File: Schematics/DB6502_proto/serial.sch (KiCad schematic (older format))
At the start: 21 parts, among them J11 LCD Port, J12 VIA Ports, U17 74AC08, U18 SC26C92, U19 65C22S, U20 74AC04, U21 74AC574, U8 74AC04, U9 74HC21, Y2 3,6864MHz

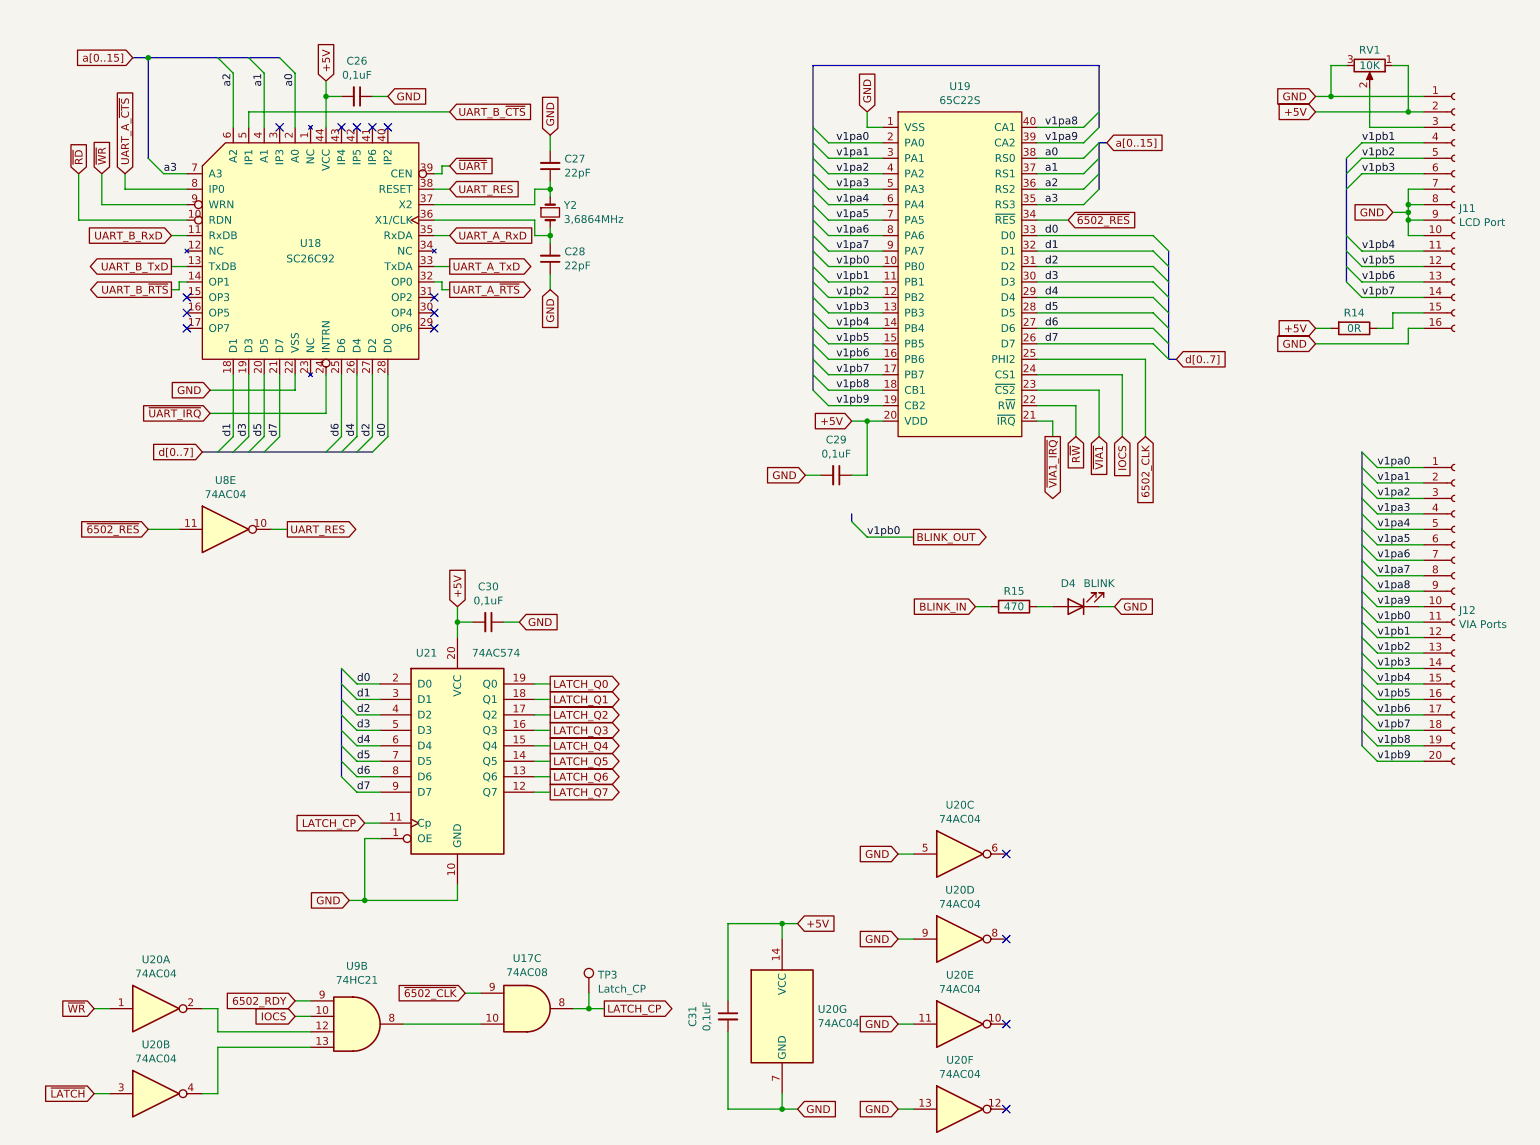
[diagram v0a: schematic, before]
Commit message: Added GPIO section
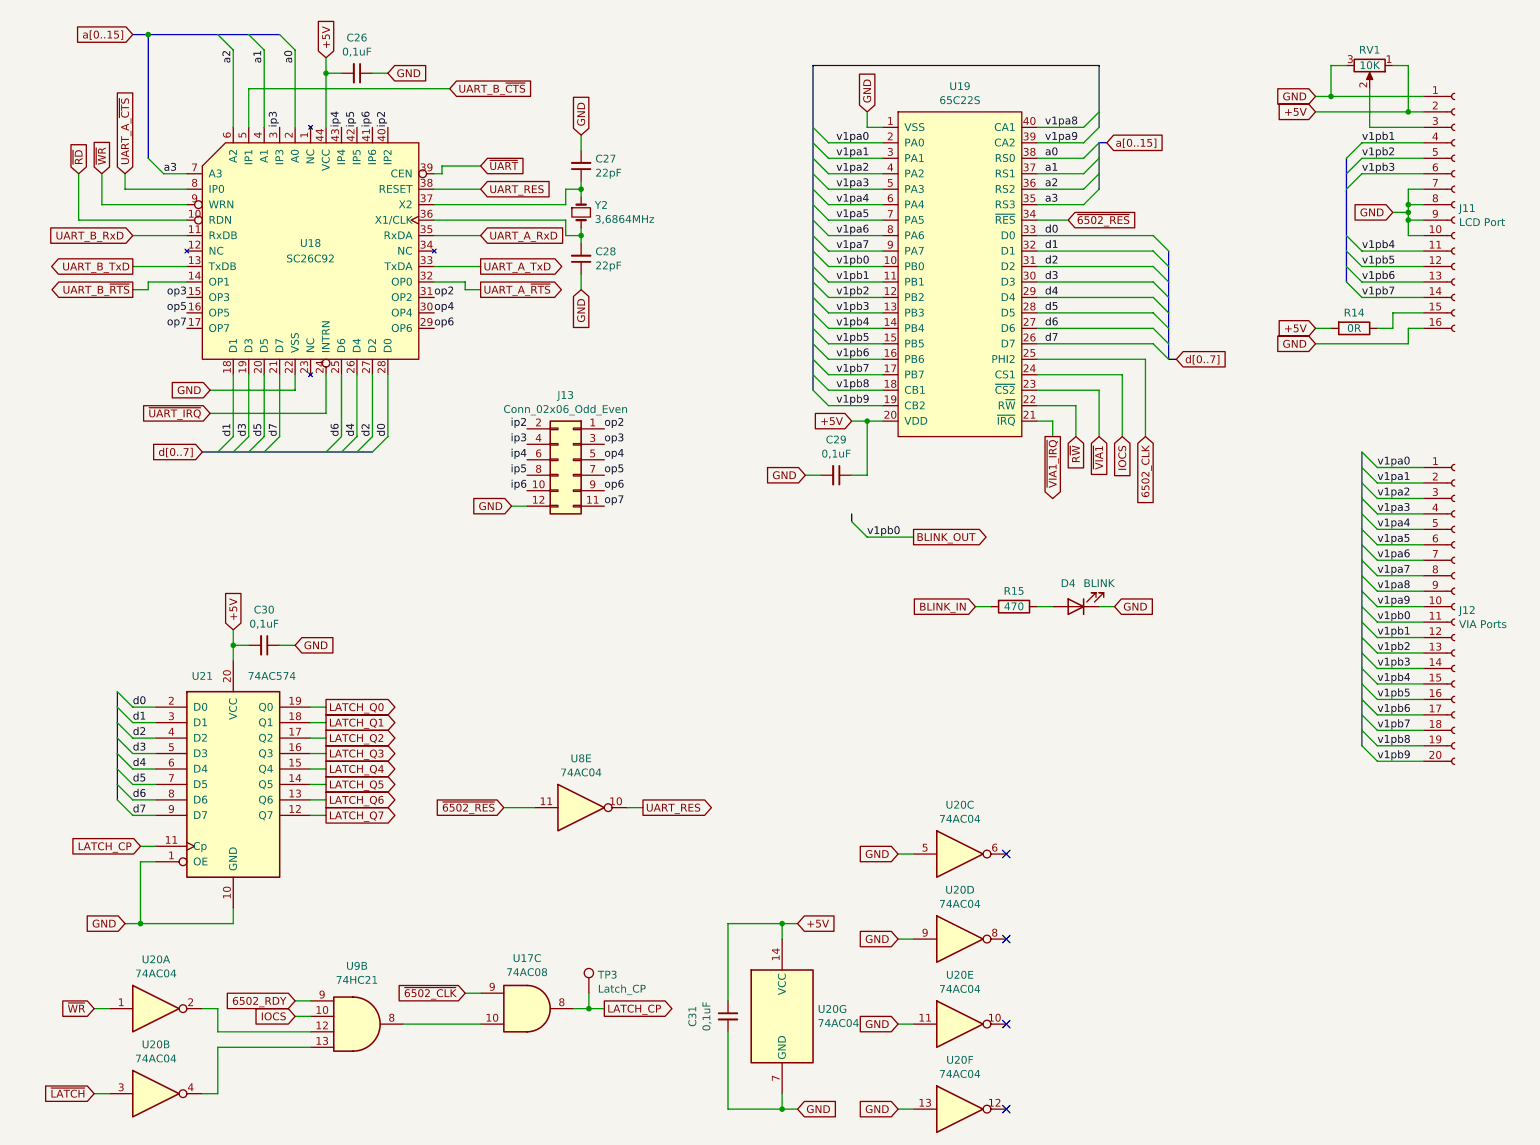
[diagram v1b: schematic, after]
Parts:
- added J13: Conn_02x06_Odd_Even, Connector_PinSocket_2.54mm:PinSocket_2x06_P2.54mm_Vertical, symbol Connector_Generic:Conn_02x06_Odd_Even
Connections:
- net GND: now also J13.12 (Pin_12)
- net op3: now reaches U18.15 (OP3)
- net op3: now also J13.3 (Pin_3)
- net op5: now reaches U18.16 (OP5)
- net op5: now also J13.7 (Pin_7)
- net op7: now reaches U18.17 (OP7)
- net op7: now also J13.11 (Pin_11)
- net op6: now reaches U18.29 (OP6)
- net op6: now also J13.9 (Pin_9)
- net ip3: now reaches U18.3 (IP3)
- net ip3: now also J13.4 (Pin_4)
- net op4: now reaches U18.30 (OP4)
- net op4: now also J13.5 (Pin_5)
- net op2: now reaches U18.31 (OP2)
- net op2: now also J13.1 (Pin_1)
- net ip2: now reaches U18.40 (IP2)
- net ip2: now also J13.2 (Pin_2)
- net ip6: now reaches U18.41 (IP6)
- net ip6: now also J13.10 (Pin_10)
- net ip5: now reaches U18.42 (IP5)
- net ip5: now also J13.8 (Pin_8)
- net ip4: now reaches U18.43 (IP4)
- net ip4: now also J13.6 (Pin_6)
- no-connect marks 15 -> 4
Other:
- moved on the sheet: C26, C27, C28, C30, U21, U8E, Y2

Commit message: Further improvements
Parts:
- J13: value Conn_02x06_Odd_Even -> UART GPIO
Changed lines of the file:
@@
 P 4100 3400
 F 0 "J13" H 4150 3817 50  0000 C CNN
-F 1 "Conn_02x06_Odd_Even" H 4150 3726 50  0000 C CNN
+F 1 "UART GPIO" H 4150 3726 50  0000 C CNN
 F 2 "Connector_PinSocket_2.54mm:PinSocket_2x06_P2.54mm_Vertical" H 4100 3400 50  0001 C CNN
 F 3 "~" H 4100 3400 50  0001 C CNN

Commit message: PCB RC2
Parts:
- C27, C28: footprint Capacitor_THT:C_Disc_D5.0mm_W2.5mm_P2.50mm -> Capacitor_SMD:C_1206_3216Metric_Pad1.33x1.80mm_HandSolder
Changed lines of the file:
@@
 F 0 "C27" H 4058 1454 50  0000 R CNN
 F 1 "22pF" H 4058 1545 50  0000 R CNN
-F 2 "Capacitor_THT:C_Disc_D5.0mm_W2.5mm_P2.50mm" H 4150 1500 50  0001 C CNN
+F 2 "Capacitor_SMD:C_1206_3216Metric_Pad1.33x1.80mm_HandSolder" H 4150 1500 50  0001 C CNN
 F 3 "~" H 4150 1500 50  0001 C CNN
 	1    4150 1500
@@
 F 0 "C28" H 4058 2054 50  0000 R CNN
 F 1 "22pF" H 4058 2145 50  0000 R CNN
-F 2 "Capacitor_THT:C_Disc_D5.0mm_W2.5mm_P2.50mm" H 4150 2100 50  0001 C CNN
+F 2 "Capacitor_SMD:C_1206_3216Metric_Pad1.33x1.80mm_HandSolder" H 4150 2100 50  0001 C CNN
 F 3 "~" H 4150 2100 50  0001 C CNN
 	1    4150 2100

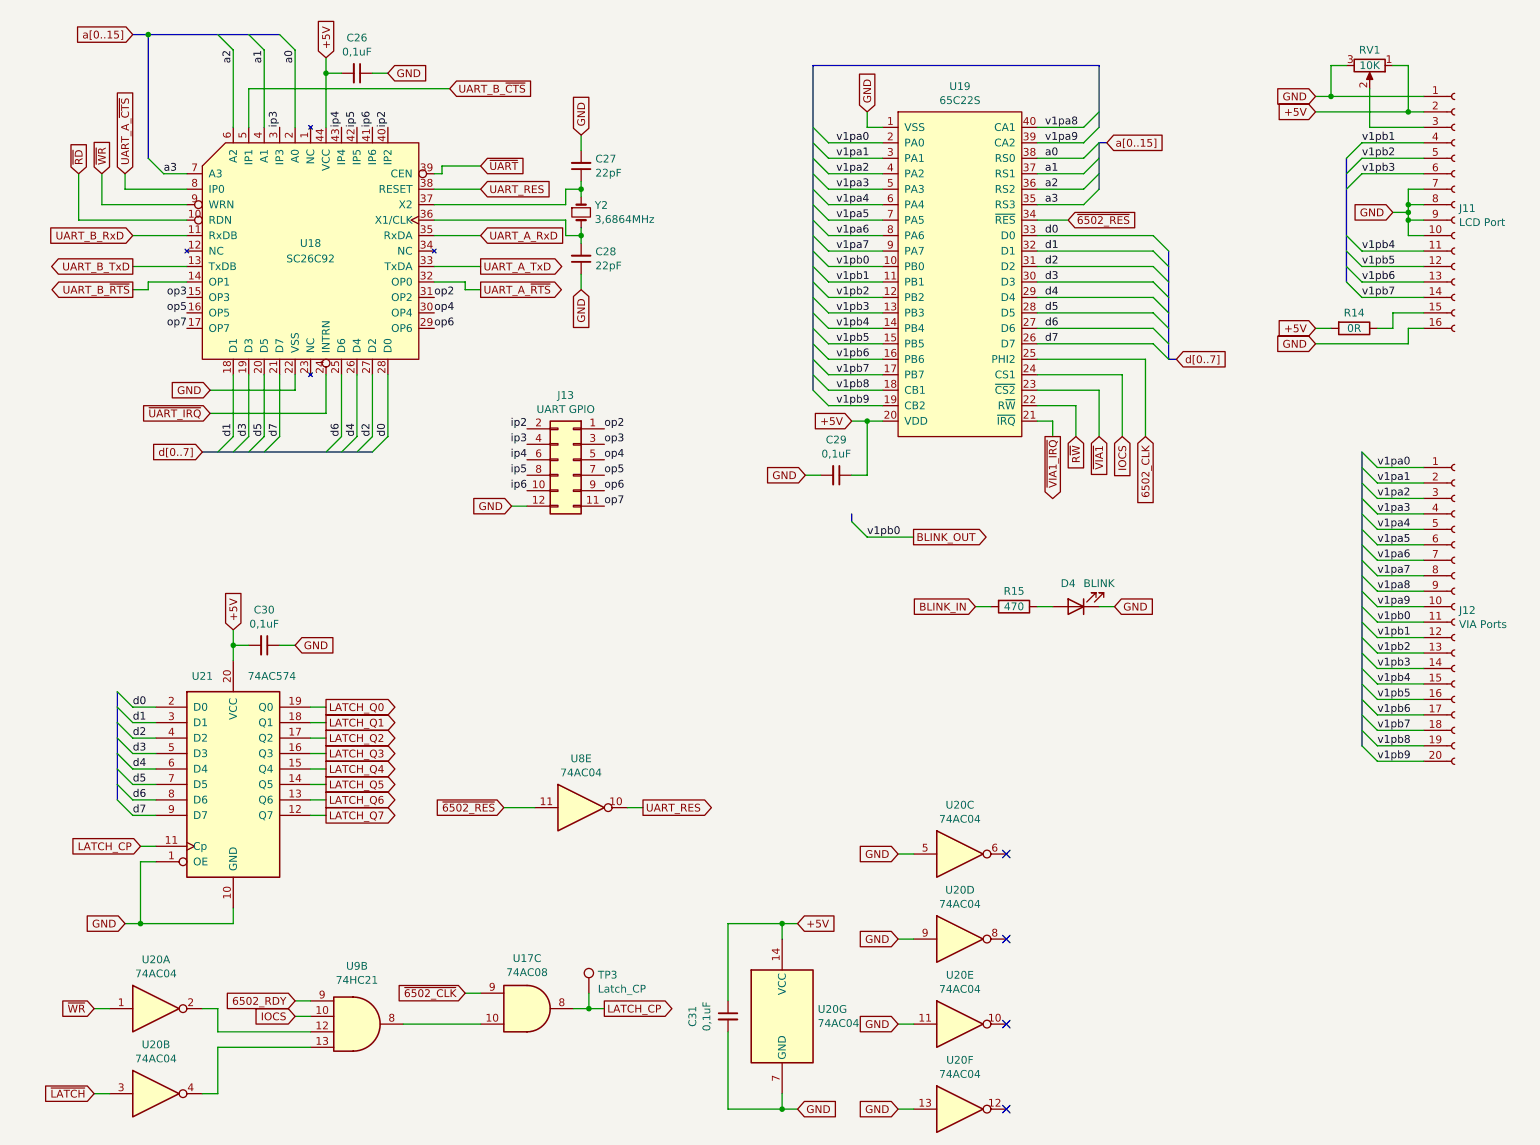
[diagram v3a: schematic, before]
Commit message: Created control plane schema
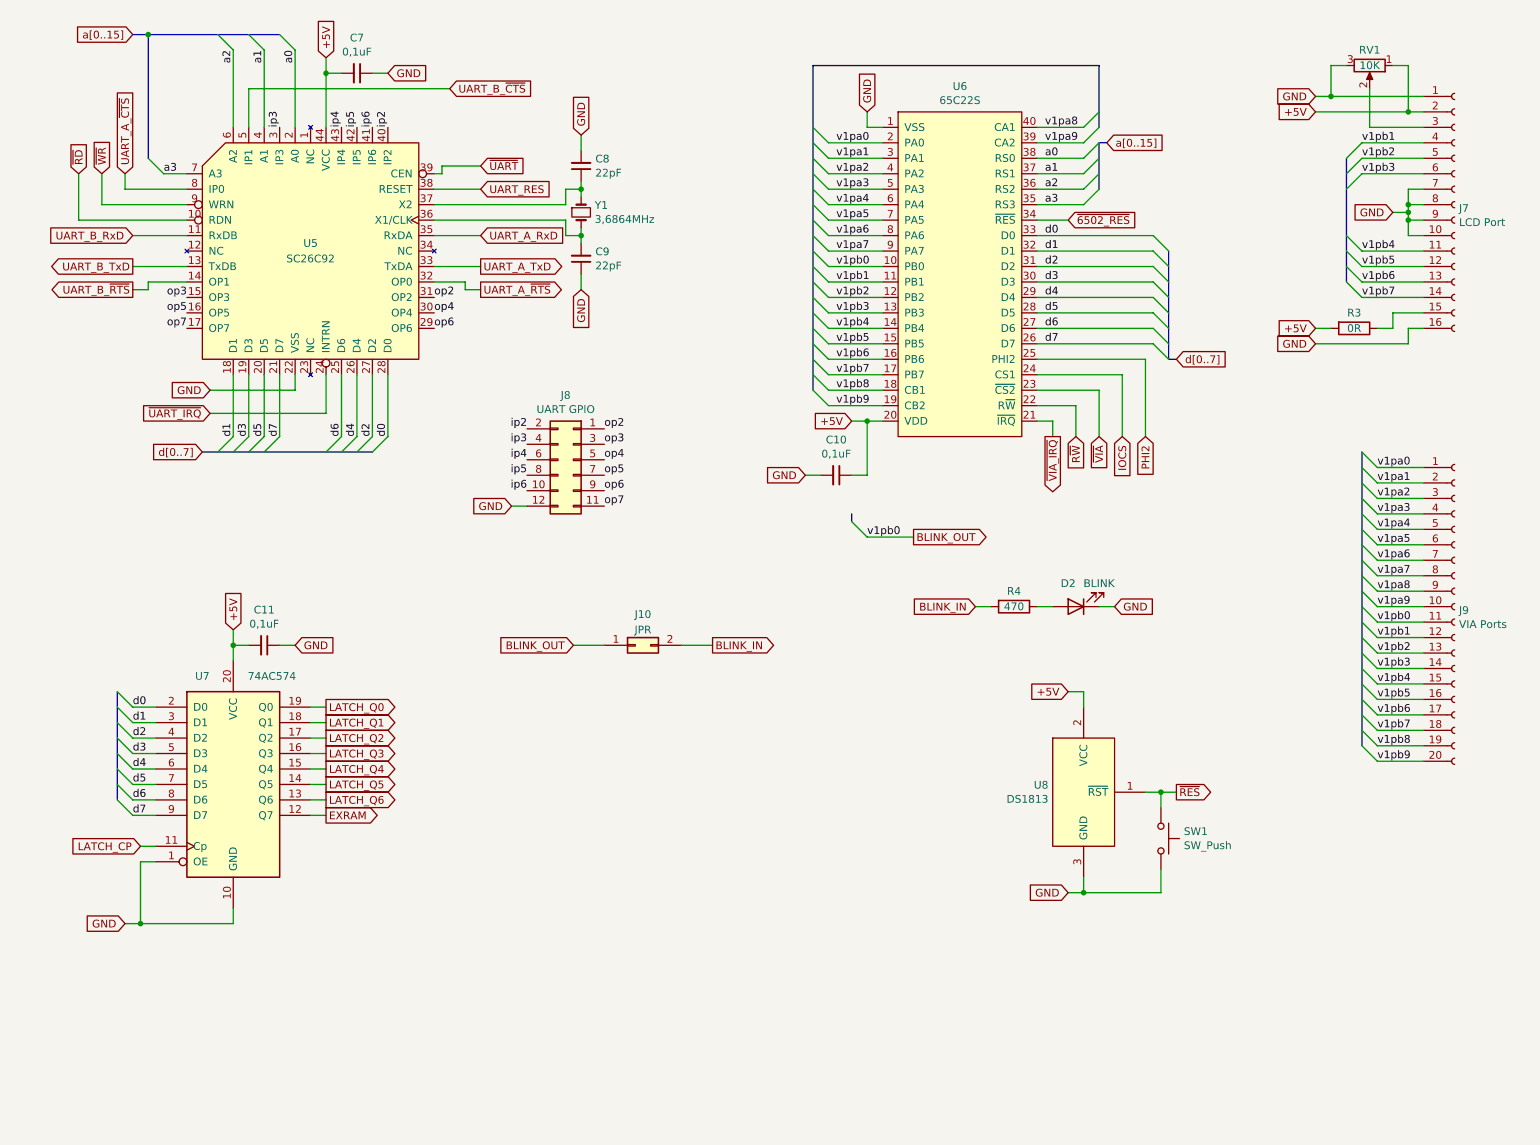
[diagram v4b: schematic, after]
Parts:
- removed C31: 0,1uF, Capacitor_SMD:C_1206_3216Metric_Pad1.42x1.75mm_HandSolder, symbol Device:C_Small
- removed TP3: Latch_CP, TestPoint:TestPoint_Keystone_5005-5009_Compact, symbol Connector:TestPoint
- removed U17: 74AC08, Package_SO:SOIC-14_3.9x8.7mm_P1.27mm, symbol 74xx:74LS08
- removed U20: 74AC04, Package_SO:SOIC-14_3.9x8.7mm_P1.27mm, symbol 74xx:74HC04
- removed U8: 74AC04, Package_SO:SOIC-14_3.9x8.7mm_P1.27mm, symbol 74xx:74LS04
- removed U9: 74HC21, Package_SO:SOIC-14_3.9x8.7mm_P1.27mm, symbol 74xx:74LS21
- added J10: JPR, Connector_PinHeader_2.54mm:PinHeader_2x01_P2.54mm_Vertical, symbol Connector_Generic:Conn_02x01
- added SW1: SW_Push, Button_Switch_THT:SW_PUSH_6mm, symbol Switch:SW_Push
- added U8: DS1813, Package_TO_SOT_THT:TO-92_Inline, symbol 6502:DS1813
- renumbered C29 to C10, C30 to C11, C26 to C7, C27 to C8, C28 to C9, D4 to D2, J11 to J7, J13 to J8, J12 to J9, R14 to R3, R15 to R4, U18 to U5, U19 to U6, U21 to U7, Y2 to Y1
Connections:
- net +5V: now also U8.2 (VCC)
- net BLINK_IN: now also J10.2 (Pin_2)
- net BLINK_OUT: now also J10.1 (Pin_1)
- net GND: now also SW1.2, U8.3 (GND)
- net 6502_CLK renamed PHI2
- net LATCH_Q7 renamed EXRAM
- net ~VIA1 renamed ~VIA
- net ~VIA1_IRQ renamed ~VIA_IRQ
- new net ~RES: SW1.1, U8.1 (~RST)
- no-connect marks 4 -> 0
